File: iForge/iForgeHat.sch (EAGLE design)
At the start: 49 parts, among them J17 CONN_12X2, J18 5.5x2.1mm Barrel, U1 ADS1015IDGST, U3 TB6621FNG

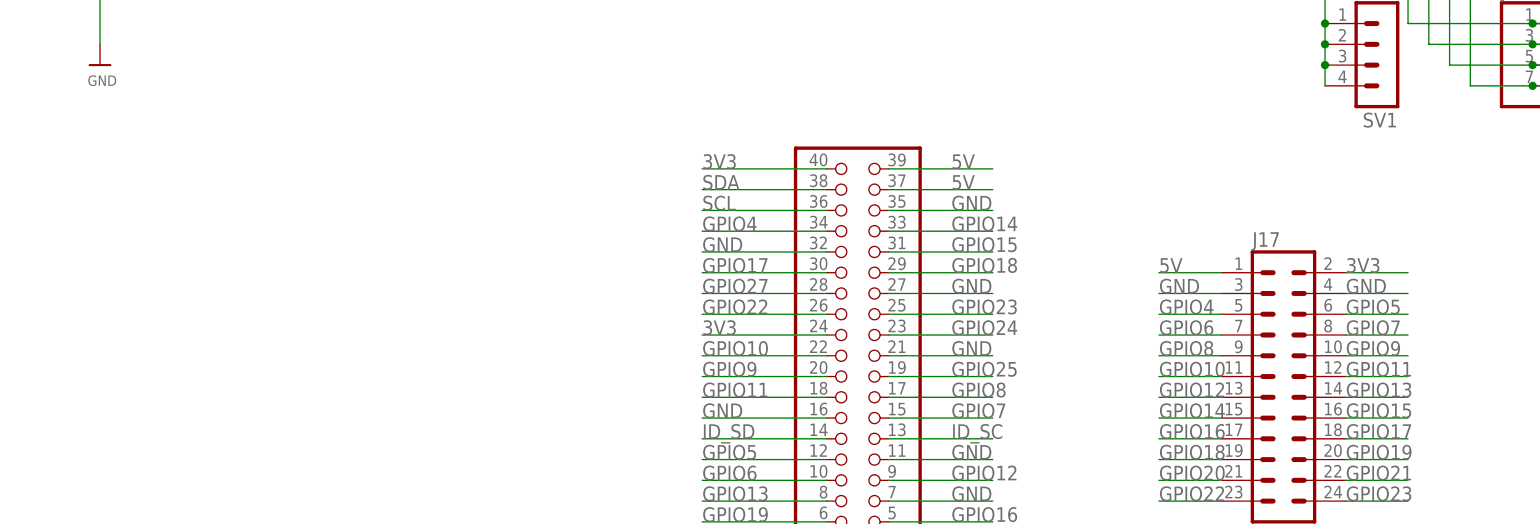
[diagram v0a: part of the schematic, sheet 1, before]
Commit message: built power management
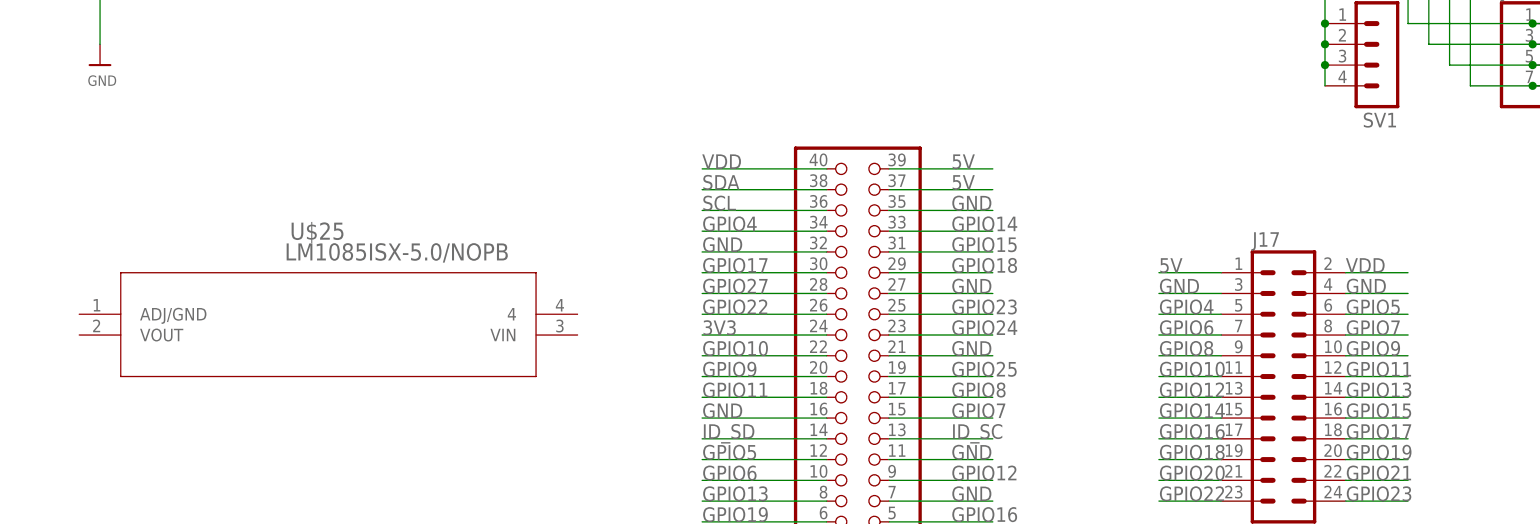
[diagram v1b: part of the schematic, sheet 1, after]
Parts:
- added U$25: LM1085ISX-5.0/NOPB, TIVoltage:LM1085ISX-5.0/NOPB
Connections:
- net 3V3: no longer J17.2, JP1.40
- net VDD: now also J17.2, JP1.40
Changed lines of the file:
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@@
 <part name="J18" library="SparkFun-Connectors" deviceset="POWER_JACK" device="SMD" value="5.5x2.1mm Barrel"/>
 <part name="FRAME2" library="frames" deviceset="FRAME_A_L" device=""/>
+<part name="U$25" library="TIVoltage" deviceset="LM1085ISX-5.0/NOPB" device=""/>
 </parts>
 <sheets>
@@
 <instance part="J17" gate="G$1" x="165.1" y="50.8"/>
 <instance part="J18" gate="G$1" x="15.24" y="12.7"/>
+<instance part="U$25" gate="A" x="10.16" y="60.96"/>
 </instances>
 <busses>
@@
 <junction x="15.24" y="147.32"/>
 </segment>
+<segment>
+<pinref part="JP1" gate="A" pin="40"/>
+<wire x1="104.14" y1="78.74" x2="88.9" y2="78.74" width="0.1524" layer="91"/>
+<label x="88.9" y="78.74" size="1.778" layer="95"/>
+</segment>
+<segment>
+<pinref part="J17" gate="G$1" pin="2"/>
+<wire x1="167.64" y1="66.04" x2="175.26" y2="66.04" width="0.1524" layer="91"/>
+<label x="167.64" y="66.04" size="1.778" layer="95"/>
+</segment>
 </net>
 <net name="N$3" class="0">
@@
 <net name="3V3" class="0">
 <segment>
-<pinref part="JP1" gate="A" pin="40"/>
-<wire x1="104.14" y1="78.74" x2="88.9" y2="78.74" width="0.1524" layer="91"/>
-<label x="88.9" y="78.74" size="1.778" layer="95"/>
-</segment>
-<segment>
 <pinref part="JP1" gate="A" pin="24"/>
 <wire x1="104.14" y1="58.42" x2="88.9" y2="58.42" width="0.1524" layer="91"/>
 <label x="88.9" y="58.42" size="1.778" layer="95"/>
 </segment>
-<segment>
-<pinref part="J17" gate="G$1" pin="2"/>
-<wire x1="167.64" y1="66.04" x2="175.26" y2="66.04" width="0.1524" layer="91"/>
-<label x="167.64" y="66.04" size="1.778" layer="95"/>
-</segment>
-</net>
+</net>

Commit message: power management
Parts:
- removed U$25: LM1085ISX-5.0/NOPB, TIVoltage:LM1085ISX-5.0/NOPB
- added C6, C7: 10 uF, SparkFun:CAP_POL1206
- added J19, JP4: (no value), jumper:J2X2MM
- added JP3: (no value), jumper:JP1E
- added U4: LM1085ISX-5.0/NOPB, TIVoltage:LM1085ISX-5.0/NOPB
- C2: value 10uF -> 10 uF; device adafruit:SUPERCAP -> SparkFun:CAP_POL1206
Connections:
- removed net VM: C2.+, C3.P$1, U3.VM1, U3.VM2, U3.VM3
- new net DCVIN: C2.+, C3.P$1, J19.2, U3.VM1, U3.VM2, U3.VM3
- new net N$22: JP3.2
- new net N$23: JP3.1
- new net REG5V: C7.+, JP4.1, U4.VOUT
- new net SVIN: JP4.2
- new net VIN: C6.+, J18.PWR, J19.1, U4.VIN
- net 5V: now also J19.3, JP4.3
- net GND: now also C6.-, C7.-, J18.GNDBREAK, U4.ADJ/GND
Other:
- note added: "JP3 Powers Pi Externally"
- note added: "JP4 Powers Servos Externally"
